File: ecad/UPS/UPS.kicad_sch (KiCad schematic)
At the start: 1 part, among them U4 STM32L152RCT6

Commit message: Cleanup
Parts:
- removed U4: STM32L152RCT6, LQFP64-10x10mm, symbol UPS:STM32L152RCT6
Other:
- added sheet controller (controller.kicad_sch)
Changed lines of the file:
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@@
 	(wire
 		(pts
-			(xy 100.33 55.88) (xy 113.03 55.88)
+			(xy 100.33 55.88) (xy 173.99 55.88)
 		)
 		(stroke
@@
 		)
 	)
-	(symbol
-		(lib_id "UPS:STM32L152RCT6")
-		(at 121.92 116.84 0)
-		(unit 1)
+	(sheet
+		(at 167.64 96.52)
+		(size 76.2 59.69)
 		(exclude_from_sim no)
 		(in_bom yes)
@@
 		(dnp no)
 		(fields_autoplaced yes)
-		(property "Reference" "U4"
-			(at 161.29 124.4599 0)
+		(stroke
+			(width 0.1524)
+			(type solid)
+		)
+		(fill
+			(color 0 0 0 0.0000)
+		)
+		(property "Sheetname" "controller"
+			(at 167.64 95.8084 0)
 			(effects
 				(font
-					(size 1.524 1.524)
+					(size 1.27 1.27)
+				)
+				(justify left bottom)
+			)
+		)
+		(property "Sheetfile" "controller.kicad_sch"
+			(at 167.64 156.7946 0)
+			(effects
+				(font
+					(size 1.27 1.27)
+				)
+				(justify left top)
+			)
+		)
+		(property "Field2" ""
+			(at 167.64 96.52 0)
+			(effects
+				(font
+					(size 1.27 1.27)
+				)
+			)
+		)
+		(pin "i2c_scl" input
+			(at 167.64 138.43 180)
+			(effects
+				(font
+					(size 1.27 1.27)
 				)
 				(justify left)
 			)
 		)
-		(property "Value" "STM32L152RCT6"
-			(at 161.29 126.9999 0)
-			(show_name yes)
+		(pin "i2c_sda" input
+			(at 167.64 130.81 180)
 			(effects
 				(font
-					(size 1.524 1.524)
+					(size 1.27 1.27)
 				)
 				(justify left)
 			)
 		)
-		(property "Footprint" "LQFP64-10x10mm"
-			(at 152.654 104.394 0)
-			(effects
-				(font
-					(size 1.27 1.27)
-					(italic yes)
-				)
-				(hide yes)
-			)
-		)
-		(property "Datasheet" "https://www.st.com/resource/en/datasheet/stm32l151rc.pdf"
-			(at 151.638 101.854 0)
-			(effects
-				(font
-					(size 1.27 1.27)
-					(italic yes)
-				)
-				(hide yes)
-			)
-		)
-		(property "Description" ""
-			(at 121.92 116.84 0)
+		(pin "vbus" input
+			(at 167.64 124.46 180)
 			(effects
 				(font
 					(size 1.27 1.27)
 				)
-				(hide yes)
+				(justify left)
 			)
 		)
 		(instances
-			(project ""
+			(project "UPS"
 				(path "/9d92b60a-4a6b-449c-b462-cab19e69d38c"
-					(reference "U4")
-					(unit 1)
+					(page "5")
 				)
 			)
@@
 	)
 	(sheet
-		(at 113.03 27.94)
+		(at 173.99 27.94)
 		(size 68.58 60.452)
 		(exclude_from_sim no)
@@
 		)
 		(property "Sheetname" "BoostConvertor"
-			(at 113.03 27.2284 0)
+			(at 173.99 27.2284 0)
 			(effects
 				(font
@@
 		)
 		(property "Sheetfile" "BoostConvertor.kicad_sch"
-			(at 113.03 88.9766 0)
+			(at 173.99 88.9766 0)
 			(effects
 				(font
@@
 		)
 		(pin "VSYS" input
-			(at 113.03 55.88 180)
+			(at 173.99 55.88 180)
 			(effects
 				(font
@@
 		)
 		(pin "5v" input
-			(at 113.03 81.28 180)
+			(at 173.99 81.28 180)
 			(effects
 				(font

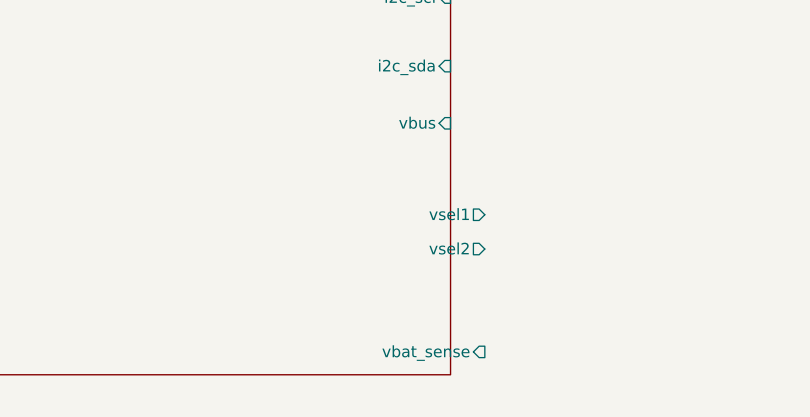
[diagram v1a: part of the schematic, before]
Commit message: added testpoint
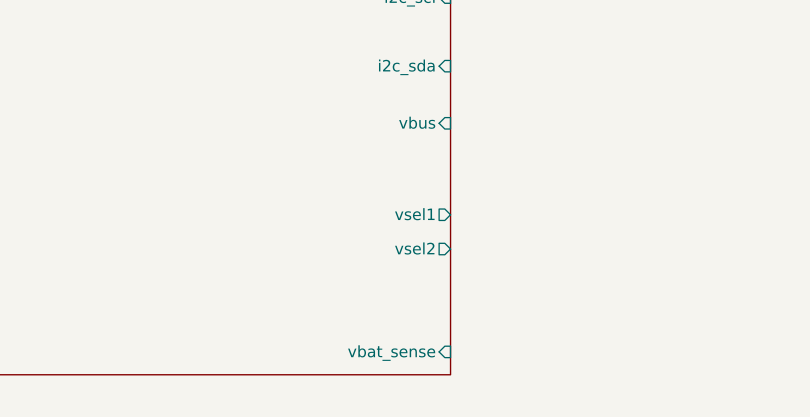
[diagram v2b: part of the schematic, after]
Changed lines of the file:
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@@
 		)
 		(pin "vbat_sense" input
-			(at 104.14 158.75 0)
+			(at 100.33 158.75 0)
 			(effects
 				(font
@@
 		)
 		(pin "vsel1" output
-			(at 104.14 143.51 0)
+			(at 100.33 143.51 0)
 			(effects
 				(font
@@
 		)
 		(pin "vsel2" output
-			(at 104.14 147.32 0)
+			(at 100.33 147.32 0)
 			(effects
 				(font

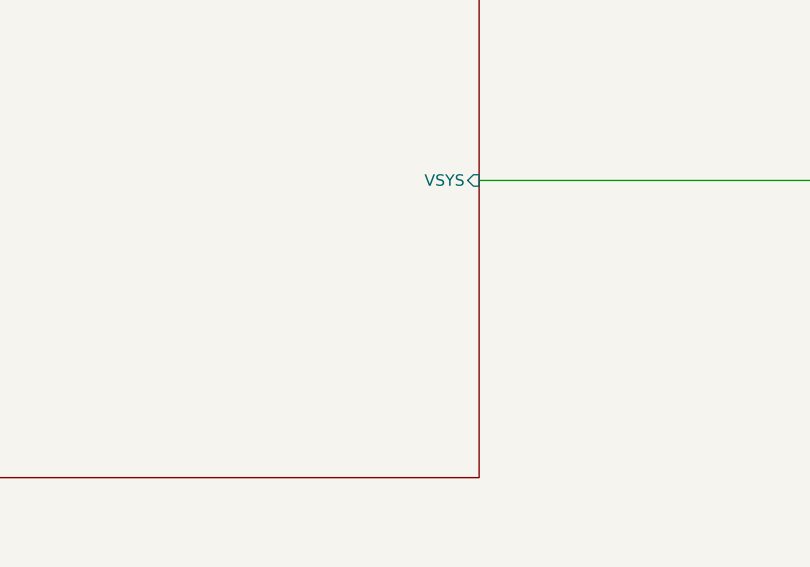
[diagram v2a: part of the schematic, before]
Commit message: Complete most of the charger schematic
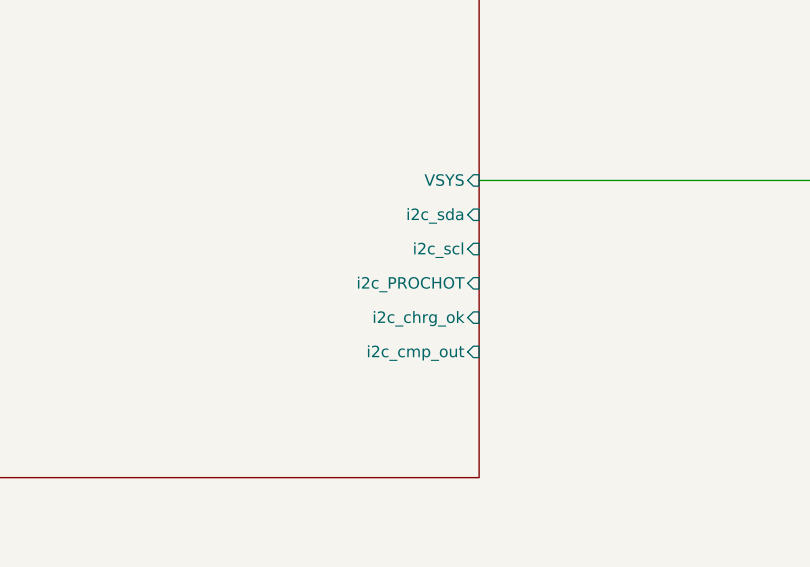
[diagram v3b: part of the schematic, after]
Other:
- sheet Charger ports: added i2c_PROCHOT, i2c_chrg_ok, i2c_cmp_out, i2c_scl, i2c_sda; removed none
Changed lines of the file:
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@@
+			)
+		)
+		(pin "i2c_sda" input
+			(at 100.33 59.69 0)
+			(effects
+				(font
+					(size 1.27 1.27)
+				)
+				(justify right)
+			)
+		)
+		(pin "i2c_scl" input
+			(at 100.33 63.5 0)
+			(effects
+				(font
+					(size 1.27 1.27)
+				)
+				(justify right)
+			)
+		)
+		(pin "i2c_PROCHOT" input
+			(at 100.33 67.31 0)
+			(effects
+				(font
+					(size 1.27 1.27)
+				)
+				(justify right)
+			)
+		)
+		(pin "i2c_chrg_ok" input
+			(at 100.33 71.12 0)
+			(effects
+				(font
+					(size 1.27 1.27)
+				)
+				(justify right)
+			)
+		)
+		(pin "i2c_cmp_out" input
+			(at 100.33 74.93 0)
+			(effects
+				(font
+					(size 1.27 1.27)
+				)
+				(justify right)
 			)
 		)
